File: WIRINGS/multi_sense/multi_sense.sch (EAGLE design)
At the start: 7 parts

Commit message: reworked structure
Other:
- note added: "WEMOS Pinning: Tx - RST - Rx - A0 - TEMT Sig D1 - D0 - D2 - D5 - PIR Sig D3 - DHT Sig D6 - D4 - D7 - DHT PWR G - D8 - TEMT PWR 5V - 3.3V - PIR PWR"
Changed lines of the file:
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@@
 <setting verticaltext="up"/>
 </settings>
-<grid distance="50" unitdist="mil" unit="mil" style="lines" multiple="1" display="no" altdistance="0.01" altunitdist="inch" altunit="inch"/>
+<grid distance="50" unitdist="mil" unit="mil" style="lines" multiple="1" display="no" altdistance="0.01" altunitdist="inch" altunit="mil"/>
 <layers>
 <layer number="1" name="Top" color="4" fill="1" visible="no" active="no"/>
@@
 <sheet>
 <plain>
+<text x="25.4" y="252.73" size="1.778" layer="91">WEMOS Pinning:
+Tx - 		RST -
+Rx - 		A0 - TEMT Sig
+D1 - 		D0 -
+D2 - 		D5 - PIR Sig
+D3 - DHT Sig                           D6 -
+D4 - 		D7 - DHT PWR
+G - 		D8 - TEMT PWR
+5V - 		3.3V - PIR PWR</text>
 </plain>
 <instances>
@@
 <net name="N$1" class="0">
 <segment>
-<wire x1="-20.32" y1="222.25" x2="-24.13" y2="222.25" width="0.1524" layer="91"/>
-<wire x1="-24.13" y1="222.25" x2="-24.13" y2="213.36" width="0.1524" layer="91"/>
 <wire x1="-24.13" y1="213.36" x2="-43.18" y2="213.36" width="0.1524" layer="91"/>
-</segment>
-</net>
-<net name="N$2" class="0">
-<segment>
+<wire x1="-24.13" y1="213.36" x2="-24.13" y2="201.93" width="0.1524" layer="91"/>
 <wire x1="-20.32" y1="201.93" x2="-21.59" y2="201.93" width="0.1524" layer="91"/>
-<wire x1="-21.59" y1="201.93" x2="-31.75" y2="201.93" width="0.1524" layer="91"/>
-<wire x1="-31.75" y1="201.93" x2="-31.75" y2="203.2" width="0.1524" layer="91"/>
-<wire x1="-31.75" y1="203.2" x2="-43.18" y2="203.2" width="0.1524" layer="91"/>
 <pinref part="R1" gate="G$1" pin="2"/>
 <wire x1="-26.67" y1="181.61" x2="-26.67" y2="176.53" width="0.1524" layer="91"/>
 <wire x1="-26.67" y1="176.53" x2="-21.59" y2="176.53" width="0.1524" layer="91"/>
 <wire x1="-21.59" y1="176.53" x2="-21.59" y2="201.93" width="0.1524" layer="91"/>
+<wire x1="-24.13" y1="201.93" x2="-21.59" y2="201.93" width="0.1524" layer="91"/>
 <junction x="-21.59" y="201.93"/>
 </segment>
@@
 </segment>
 </net>
+<net name="N$9" class="0">
+<segment>
+<wire x1="-31.75" y1="203.2" x2="-43.18" y2="203.2" width="0.1524" layer="91"/>
+<wire x1="-31.75" y1="203.2" x2="-31.75" y2="222.25" width="0.1524" layer="91"/>
+<wire x1="-31.75" y1="222.25" x2="-20.32" y2="222.25" width="0.1524" layer="91"/>
+</segment>
+</net>
 </nets>
 </sheet>
@@
 </drawing>
 <compatibility>
+<note version="6.3" minversion="6.2.2" severity="warning">
+Since Version 6.2.2 text objects can contain more than one line,
+which will not be processed correctly with this version.
+</note>
 <note version="8.2" severity="warning">
 Since Version 8.2, EAGLE supports online libraries. The ids

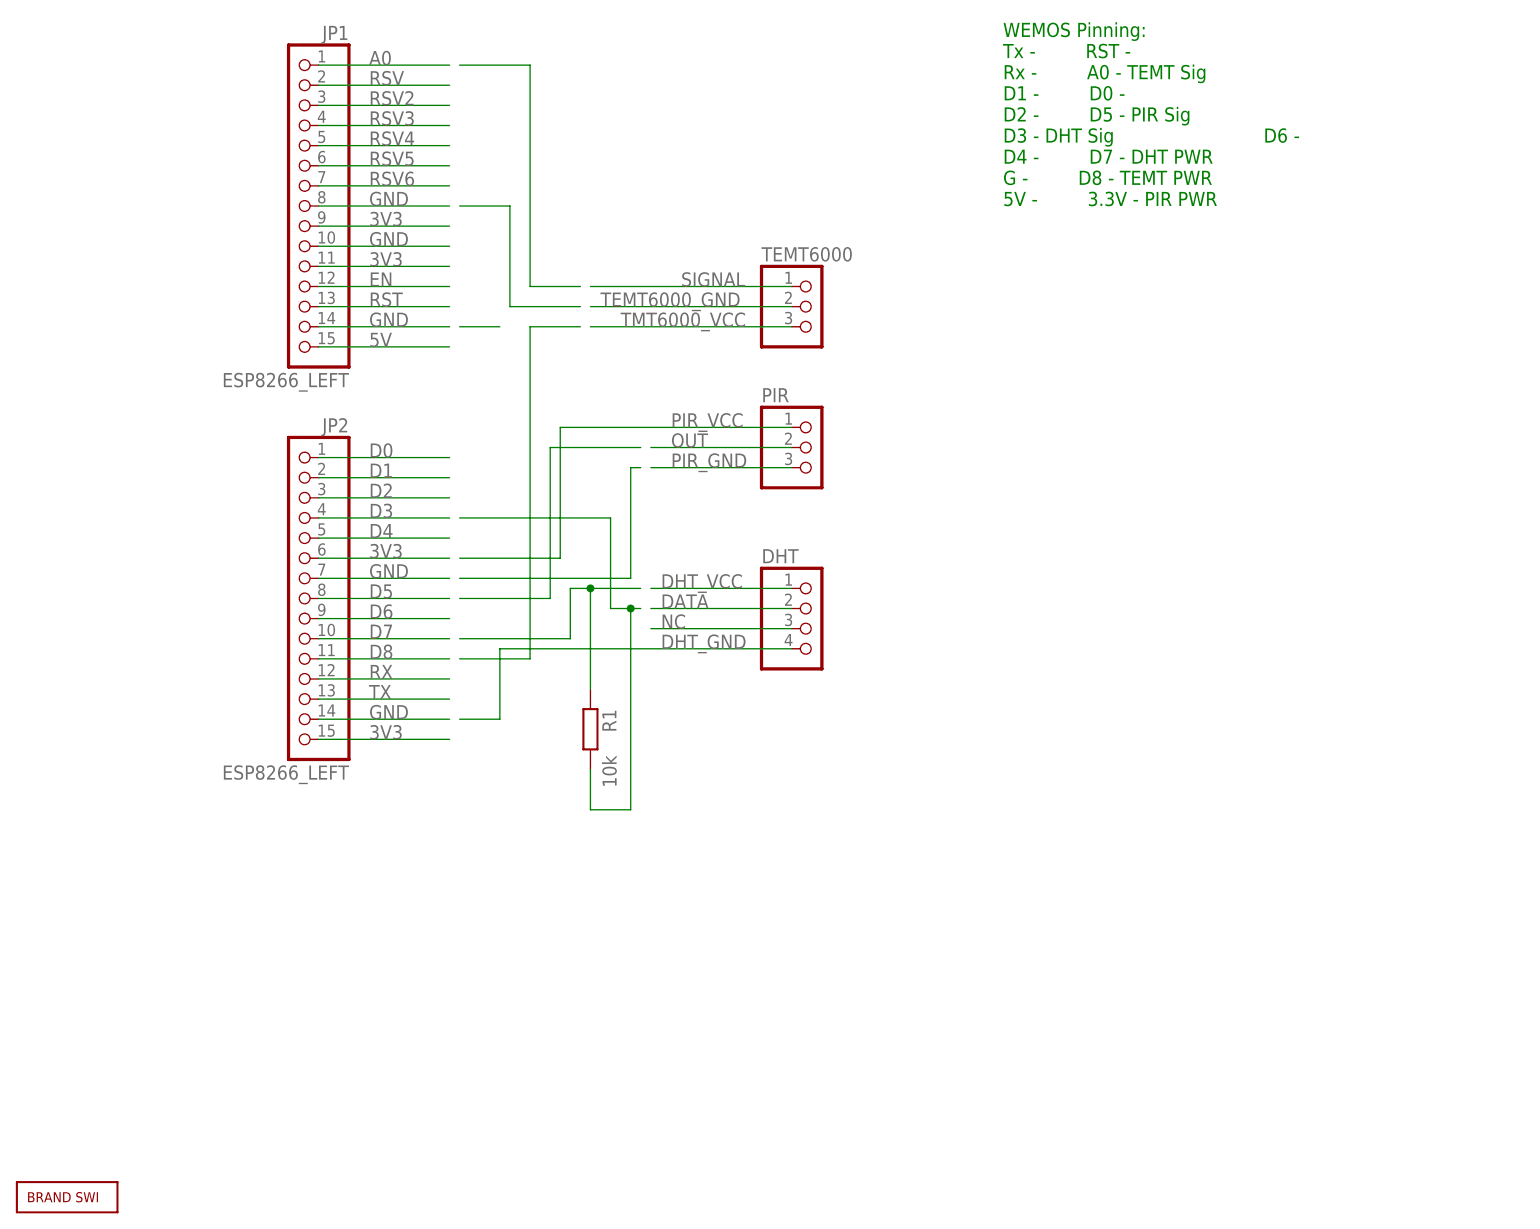
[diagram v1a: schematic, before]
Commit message: updated wemos and diverse boards
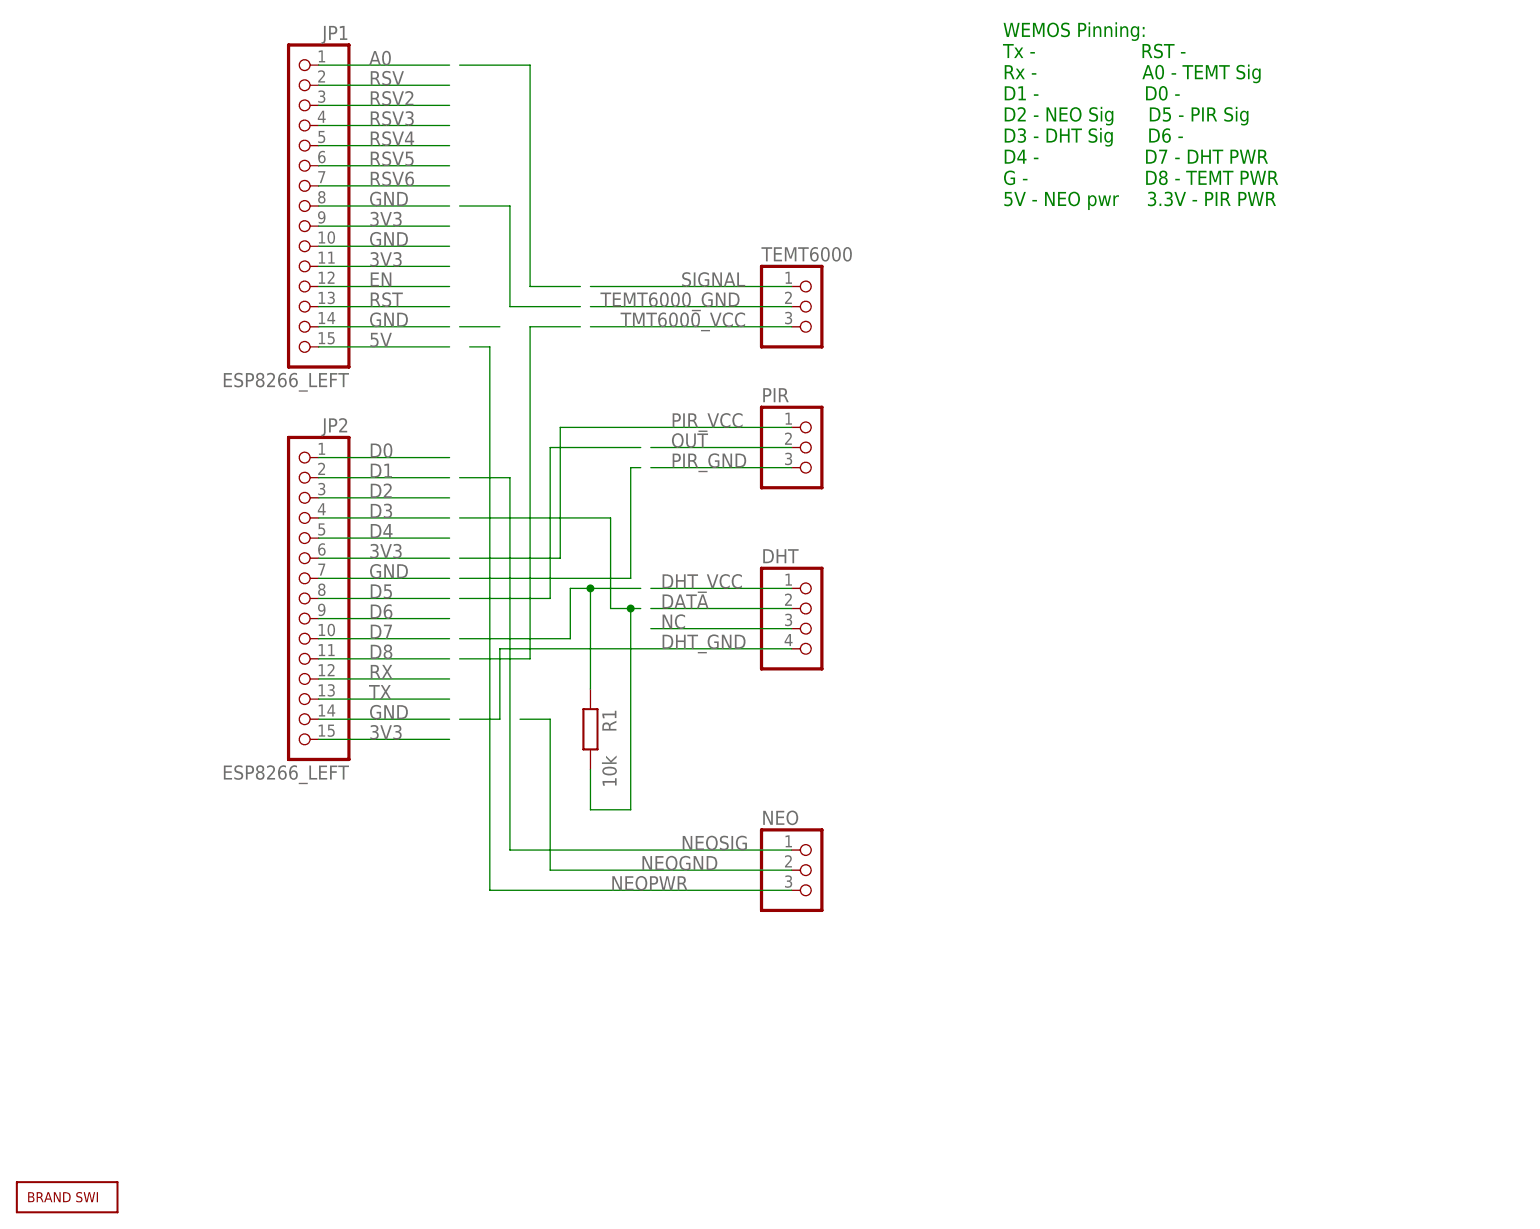
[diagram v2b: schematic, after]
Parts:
- added NEO: (no value), pinhead:PINHD-1X3
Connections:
- new net NEOGND: NEO.2
- new net NEOPWR: NEO.3
- new net NEOSIG: NEO.1
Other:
- note added: "WEMOS Pinning: Tx - RST - Rx - A0 - TEMT Sig D1 - D0 - D2 - NEO Sig D5 - PIR Sig D3 - DHT Sig D6 - D4 - D7 - DHT PWR G - D8 - TEMT PWR 5V - NEO pwr 3.3V - PIR PWR"
- note removed: "WEMOS Pinning: Tx - RST - Rx - A0 - TEMT Sig D1 - D0 - D2 - D5 - PIR Sig D3 - DHT Sig D6 - D4 - D7 - DHT PWR G - D8 - TEMT PWR 5V - 3.3V - PIR PWR"
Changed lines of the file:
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@@
 <?xml version="1.0" encoding="utf-8"?>
 <!DOCTYPE eagle SYSTEM "eagle.dtd">
-<eagle version="8.3.2">
+<eagle version="9.6.2">
 <drawing>
 <settings>
@@
 <setting verticaltext="up"/>
 </settings>
-<grid distance="50" unitdist="mil" unit="mil" style="lines" multiple="1" display="no" altdistance="0.01" altunitdist="inch" altunit="mil"/>
+<grid distance="50" unitdist="mil" unit="mil" style="lines" multiple="1" display="no" altdistance="0.01" altunitdist="inch" altunit="inch"/>
 <layers>
 <layer number="1" name="Top" color="4" fill="1" visible="no" active="no"/>
@@
 <part name="JP1" library="pinhead" library_urn="urn:adsk.eagle:library:325" deviceset="PINHD-1X15" device="" package3d_urn="urn:adsk.eagle:package:22424/1" value="ESP8266_LEFT"/>
 <part name="JP2" library="pinhead" library_urn="urn:adsk.eagle:library:325" deviceset="PINHD-1X15" device="" package3d_urn="urn:adsk.eagle:package:22424/1" value="ESP8266_LEFT"/>
+<part name="NEO" library="pinhead" library_urn="urn:adsk.eagle:library:325" deviceset="PINHD-1X3" device="" package3d_urn="urn:adsk.eagle:package:22458/2"/>
 </parts>
 <sheets>
@@
 <plain>
 <text x="25.4" y="252.73" size="1.778" layer="91">WEMOS Pinning:
-Tx - 		RST -
-Rx - 		A0 - TEMT Sig
-D1 - 		D0 -
-D2 - 		D5 - PIR Sig
-D3 - DHT Sig                           D6 -
-D4 - 		D7 - DHT PWR
-G - 		D8 - TEMT PWR
-5V - 		3.3V - PIR PWR</text>
+Tx -                   RST -
+Rx -                   A0 - TEMT Sig
+D1 -                   D0 -
+D2 - NEO Sig      D5 - PIR Sig
+D3 - DHT Sig      D6 -
+D4 -                   D7 - DHT PWR
+G -                     D8 - TEMT PWR
+5V - NEO pwr     3.3V - PIR PWR</text>
 </plain>
 <instances>
-<instance part="FRAME1" gate="G$1" x="-114.3" y="111.76"/>
-<instance part="U$2" gate="G$1" x="-99.06" y="125.73"/>
+<instance part="FRAME1" gate="G$1" x="-114.3" y="111.76" smashed="yes">
+<attribute name="DRAWING_NAME" x="102.87" y="127" size="2.54" layer="94"/>
+<attribute name="LAST_DATE_TIME" x="102.87" y="121.92" size="2.286" layer="94"/>
+<attribute name="SHEET" x="116.205" y="116.84" size="2.54" layer="94"/>
+</instance>
+<instance part="U$2" gate="G$1" x="-99.06" y="125.73" smashed="yes"/>
 <instance part="R1" gate="G$1" x="-26.67" y="186.69" smashed="yes" rot="R270">
 <attribute name="NAME" x="-25.1714" y="189.23" size="1.778" layer="95" rot="R270"/>
 <attribute name="VALUE" x="-25.146" y="183.388" size="1.778" layer="96" rot="R270"/>
 </instance>
-<instance part="PIR" gate="A" x="1.27" y="222.25"/>
-<instance part="DHT" gate="A" x="1.27" y="199.39"/>
-<instance part="TEMT6000" gate="A" x="1.27" y="240.03"/>
-<instance part="JP1" gate="A" x="-63.5" y="252.73" rot="MR0"/>
-<instance part="JP2" gate="A" x="-63.5" y="203.2" rot="MR0"/>
+<instance part="PIR" gate="A" x="1.27" y="222.25" smashed="yes">
+<attribute name="NAME" x="-5.08" y="227.965" size="1.778" layer="95"/>
+<attribute name="VALUE" x="-5.08" y="214.63" size="1.778" layer="96"/>
+</instance>
+<instance part="DHT" gate="A" x="1.27" y="199.39" smashed="yes">
+<attribute name="NAME" x="-5.08" y="207.645" size="1.778" layer="95"/>
+<attribute name="VALUE" x="-5.08" y="191.77" size="1.778" layer="96"/>
+</instance>
+<instance part="TEMT6000" gate="A" x="1.27" y="240.03" smashed="yes">
+<attribute name="NAME" x="-5.08" y="245.745" size="1.778" layer="95"/>
+<attribute name="VALUE" x="-5.08" y="232.41" size="1.778" layer="96"/>
+</instance>
+<instance part="JP1" gate="A" x="-63.5" y="252.73" smashed="yes" rot="MR0">
+<attribute name="NAME" x="-57.15" y="273.685" size="1.778" layer="95" rot="MR0"/>
+<attribute name="VALUE" x="-57.15" y="229.87" size="1.778" layer="96" rot="MR0"/>
+</instance>
+<instance part="JP2" gate="A" x="-63.5" y="203.2" smashed="yes" rot="MR0">
+<attribute name="NAME" x="-57.15" y="224.155" size="1.778" layer="95" rot="MR0"/>
+<attribute name="VALUE" x="-57.15" y="180.34" size="1.778" layer="96" rot="MR0"/>
+</instance>
+<instance part="NEO" gate="A" x="1.27" y="168.91" smashed="yes">
+<attribute name="NAME" x="-5.08" y="174.625" size="1.778" layer="95"/>
+<attribute name="VALUE" x="-5.08" y="161.29" size="1.778" layer="96"/>
+</instance>
 </instances>
 <busses>
@@
 </segment>
 </net>
+<net name="NEOSIG" class="0">
+<segment>
+<pinref part="NEO" gate="A" pin="1"/>
+<wire x1="-1.27" y1="171.45" x2="-36.83" y2="171.45" width="0.1524" layer="91"/>
+<wire x1="-36.83" y1="171.45" x2="-36.83" y2="218.44" width="0.1524" layer="91"/>
+<wire x1="-36.83" y1="218.44" x2="-43.18" y2="218.44" width="0.1524" layer="91"/>
+<label x="-15.24" y="171.45" size="1.778" layer="95"/>
+</segment>
+</net>
+<net name="NEOGND" class="0">
+<segment>
+<pinref part="NEO" gate="A" pin="2"/>
+<wire x1="-1.27" y1="168.91" x2="-31.75" y2="168.91" width="0.1524" layer="91"/>
+<wire x1="-31.75" y1="168.91" x2="-31.75" y2="187.96" width="0.1524" layer="91"/>
+<wire x1="-31.75" y1="187.96" x2="-35.56" y2="187.96" width="0.1524" layer="91"/>
+<label x="-20.32" y="168.91" size="1.778" layer="95"/>
+</segment>
+</net>
+<net name="NEOPWR" class="0">
+<segment>
+<pinref part="NEO" gate="A" pin="3"/>
+<wire x1="-1.27" y1="166.37" x2="-39.37" y2="166.37" width="0.1524" layer="91"/>
+<wire x1="-39.37" y1="166.37" x2="-39.37" y2="234.95" width="0.1524" layer="91"/>
+<wire x1="-39.37" y1="234.95" x2="-41.91" y2="234.95" width="0.1524" layer="91"/>
+<label x="-24.13" y="166.37" size="1.778" layer="95"/>
+</segment>
+</net>
